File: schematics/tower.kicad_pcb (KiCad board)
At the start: 2 copper layers, 50.8 x 48.3 mm, 17 parts, among them IC1 ESP32-SOLO-1, J1 Conn_01x02, J2 Conn_01x06, J3 Conn_01x09, J4 Conn_02x10_Odd_Even, SW1 SW_Push, SW2 SW_SPDT, U1 NCP1117-3.3_SOT223

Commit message: finished (I think) schematics for tower and controller
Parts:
- removed the REF** at (127.0, 119.4)
- removed the REF** at (170.2, 116.8)
- removed the REF** at (127.0, 80.0)
- removed U1: NCP1117-3.3_SOT223, Package_TO_SOT_SMD:SOT-223-3_TabPin2
- added C5: 100nF, Capacitor_SMD:C_0805_2012Metric, B.Cu at (150.4, 61.5)
- added C6: 100nF, Capacitor_SMD:C_0805_2012Metric, F.Cu at (186.7, 58.4)
- added C7: 100nF, Capacitor_SMD:C_0805_2012Metric, F.Cu at (180.3, 86.4)
- added D1: BAT760-7, Mouser:SOD2513X120N, F.Cu at (125.7, 68.6)
- added D2: LED, Mouser:APHCM2012QBCDF01, F.Cu at (118.6, 65.5)
- added J5: Conn_02x10_Odd_Even, Connector_PinSocket_2.54mm:PinSocket_2x10_P2.54mm_Vertical, F.Cu at (188.0, 62.2)
- added Q1: SS8050-G, Mouser:SOT95P240X115-3N, F.Cu at (152.4, 82.5)
- added Q2: SS8050-G, Mouser:SOT95P240X115-3N, F.Cu at (157.5, 82.5)
- added R3: 10k, Resistor_SMD:R_0805_2012Metric, F.Cu at (154.9, 86.4)
- added R4: 10k, Resistor_SMD:R_0805_2012Metric, F.Cu at (139.7, 66.0)
- added R5: 10k, Resistor_SMD:R_0805_2012Metric, F.Cu at (139.7, 58.4)
- added R6: 0, Resistor_SMD:R_0201_0603Metric, F.Cu at (121.9, 65.0)
- added R7: 0, Resistor_SMD:R_0201_0603Metric, F.Cu at (130.8, 62.2)
- added REF**: MountingHole_3.2mm_M3, MountingHole:MountingHole_3.2mm_M3, F.Cu at (133.3, 71.9)
- added REF**: MountingHole_3.2mm_M3, MountingHole:MountingHole_3.2mm_M3, F.Cu at (197.4, 61.5)
- added REF**: MountingHole_3.2mm_M3, MountingHole:MountingHole_3.2mm_M3, F.Cu at (197.1, 110.5)
- added REF**: MountingHole_3.2mm_M3, MountingHole:MountingHole_3.2mm_M3, F.Cu at (107.7, 110.5)
- C1, C2: value 100nF -> 0.1uF
- C4: value 100nF -> 22uF; moved to B.Cu
- IC1: footprint RF_Module:ESP32-WROOM-32 -> Mouser:ESP32SOLO1
- J1: value Conn_01x02 -> 216990-0003; footprint Connector_PinHeader_1.00mm:PinHeader_1x02_P1.00mm_Vertical -> Mouser:2169900003
- J3: value Conn_01x09 -> Conn_01x05; footprint Connector_PinSocket_1.00mm:PinSocket_1x09_P1.00mm_Vertical -> Connector_PinSocket_2.54mm:PinSocket_1x05_P2.54mm_Vertical
- J4: value Conn_02x10_Odd_Even -> SD_Card; footprint Connector_PinSocket_2.54mm:PinSocket_2x10_P2.54mm_Vertical -> Connector_Card:SD_Kyocera_145638109211859+
- R1: value 10k -> 20
- SW1: footprint Button_Switch_THT:SW_TH_Tactile_Omron_B3F-10xx -> Button_Switch_SMD:SW_SPST_CK_KXT3
- SW2: value SW_SPDT -> SW_Push; footprint Button_Switch_THT:SW_Slide_1P2T_CK_OS102011MS2Q -> Button_Switch_SMD:SW_SPST_CK_KXT3
- moved J4 57.5 mm to (114.3, 92.7), turned to 270 degrees
- moved C4 50.1 mm to (150.4, 58.4), turned to 0 degrees
- moved J1 40.6 mm to (107.4, 66.0), turned to 270 degrees
- moved C3 38.9 mm to (139.7, 62.2)
- moved R1 37.3 mm to (119.4, 68.6), turned to 180 degrees
- moved SW1 30.1 mm to (165.1, 82.5), turned to 180 degrees
- moved C1 28.5 mm to (165.1, 88.9), turned to 0 degrees
- moved SW2 28.0 mm to (144.8, 82.5), turned to 0 degrees
- moved J2 27.9 mm to (152.4, 97.8), turned to 90 degrees
- moved J3 26.2 mm to (121.9, 59.7), turned to 90 degrees
- moved IC1 24.4 mm to (154.9, 63.5)
- moved C2 17.3 mm to (144.8, 88.9)
- moved R2 14.0 mm to (154.9, 90.2)
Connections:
- net AUDIO_L renamed Net-(J4-Pad9)
- C1 pad 1: GND -> GPIO0
- C1 pad 2: Net-(C1-Pad2) -> GND
- C2 pad 1: GND -> EN
- C2 pad 2: Vcc -> GND
- C3 pad 1: GND -> EN
- C3 pad 2: Vcc -> GND
- C4 pad 1: GND -> VOUT
- C4 pad 2: 5V -> GND
- IC1 pad 10: IO25 -> SDMOSI
- IC1 pad 11: IO26 -> SDCLK
- IC1 pad 12: IO27 -> SDMISO
- IC1 pad 13: PDN -> Net-(IC1-Pad13)
- IC1 pad 2: Vcc -> VOUT
- IC1 pad 23: GPIO2 -> Net-(IC1-Pad23)
- IC1 pad 24: Net-(IC1-Pad24) -> GPIO2
- IC1 pad 25: Net-(IC1-Pad25) -> GPIO0
- IC1 pad 26: Net-(IC1-Pad26) -> GPIO1
- IC1 pad 28: DTR -> Net-(IC1-Pad28)
- IC1 pad 29: CTS -> Net-(IC1-Pad29)
- IC1 pad 3: Net-(C1-Pad2) -> EN
- IC1 pad 36: GPIO1 -> Net-(IC1-Pad36)
- J2 pad 3: Vcc -> VOUT
- J3 pad 1: Vcc -> VOUT
- J3 pad 3: IO34 -> 5V
- J3 pad 4: IO35 -> SHDN
- J3 pad 5: IO32 -> PG
- J4 pad 1: Vcc -> Net-(J4-Pad1)
- J4 pad 10: NC -> Net-(J4-Pad10)
- J4 pad 11: GPIO0 -> Net-(J4-Pad11)
- J4 pad 12: GPIO1 -> Net-(J4-Pad12)
- J4 pad 13: GPIO2 -> Net-(J4-Pad13)
- J4 pad 2: GND -> SDMOSI
- J4 pad 3: SCK -> GND
- J4 pad 4: MISO -> VOUT
- J4 pad 5: MOSI -> SDCLK
- J4 pad 6: CS -> GND
- J4 pad 7: INT -> SDMISO
- J4 pad 8: PDN -> Net-(J4-Pad8)
- R1 pad 1: Net-(C1-Pad2) -> Net-(D1-Pad2)
- R1 pad 2: Vcc -> Net-(J1-PadA4)
- R2 pad 1: Net-(IC1-Pad25) -> DTR
- R2 pad 2: Net-(R2-Pad2) -> Net-(Q1-Pad1)
- SW1 pad 2: Vcc -> GPIO0
- SW2 pad 1: Net-(R2-Pad2) -> GND
- SW2 pad 2: Vcc -> EN
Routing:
- net GND: track 161.6 -> 14.6 mm, vias 5 -> 9
- net VOUT: track 0.00 -> 146.3 mm, vias 0 -> 5
- net Vcc: track 136.8 -> 0.00 mm, vias 1 -> 0
- net 5V: track 59.5 -> 126.9 mm, vias 0 -> 2
- net EN: track 0.00 -> 47.6 mm
- net SDMISO: track 0.00 -> 41.3 mm, vias 0 -> 2
- net SDCLK: track 0.00 -> 34.8 mm, vias 0 -> 2
- net PDN: track 32.9 -> 0.00 mm, vias 1 -> 0
- net GPIO0: track 31.6 -> 62.7 mm, vias 2 -> 0
- net SDMOSI: track 0.00 -> 28.6 mm, vias 0 -> 2
- net Net-(C1-Pad2): track 27.7 -> 0.00 mm, vias 2 -> 0
- net TX: track 18.2 -> 41.2 mm, vias 0 -> 1
- net RX: track 18.3 -> 39.5 mm, vias 0 -> 1
- net DTR: track 0.00 -> 15.8 mm
- net Net-(R2-Pad2): track 15.7 -> 0.00 mm, vias 1 -> 0
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- added copper zone on B.Cu, net GND
- added copper zone on F.Cu, net GND
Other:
- board size 50.8 x 48.3 mm -> 100.1 x 58.2 mm
- board text added: "+"
- board text added: "-"
- board text added: "5V"
- board text added: "GND"
- board text added: "PG"
- board text added: "Purdue University ECE 477: Senior Design Group 6: Mario Kart 3/1/2022 Tower PCB Version: 1.0 Authors: Andre Hatushikano Da Yeon Nam Jake Doan Jorge Apolo"
- board text added: "VOUT"

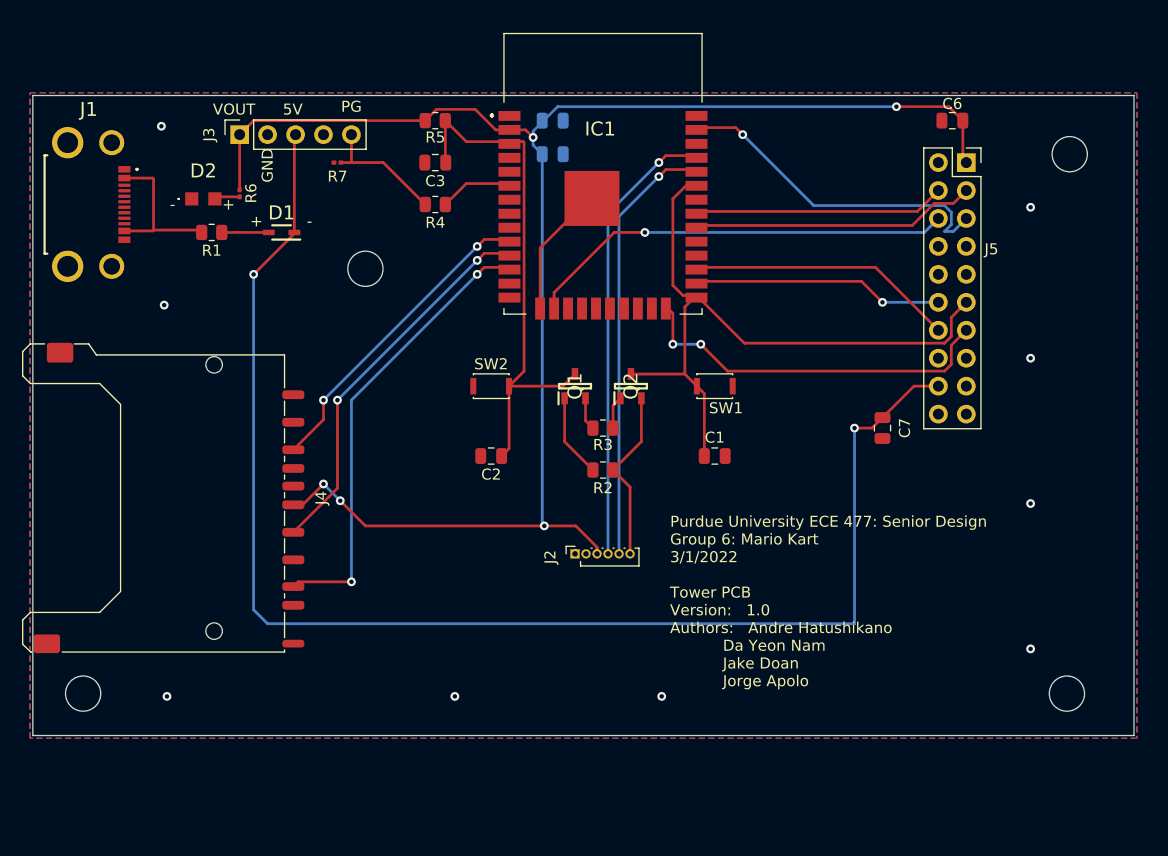
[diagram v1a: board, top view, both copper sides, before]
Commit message: converted all schematics into kicad6 format
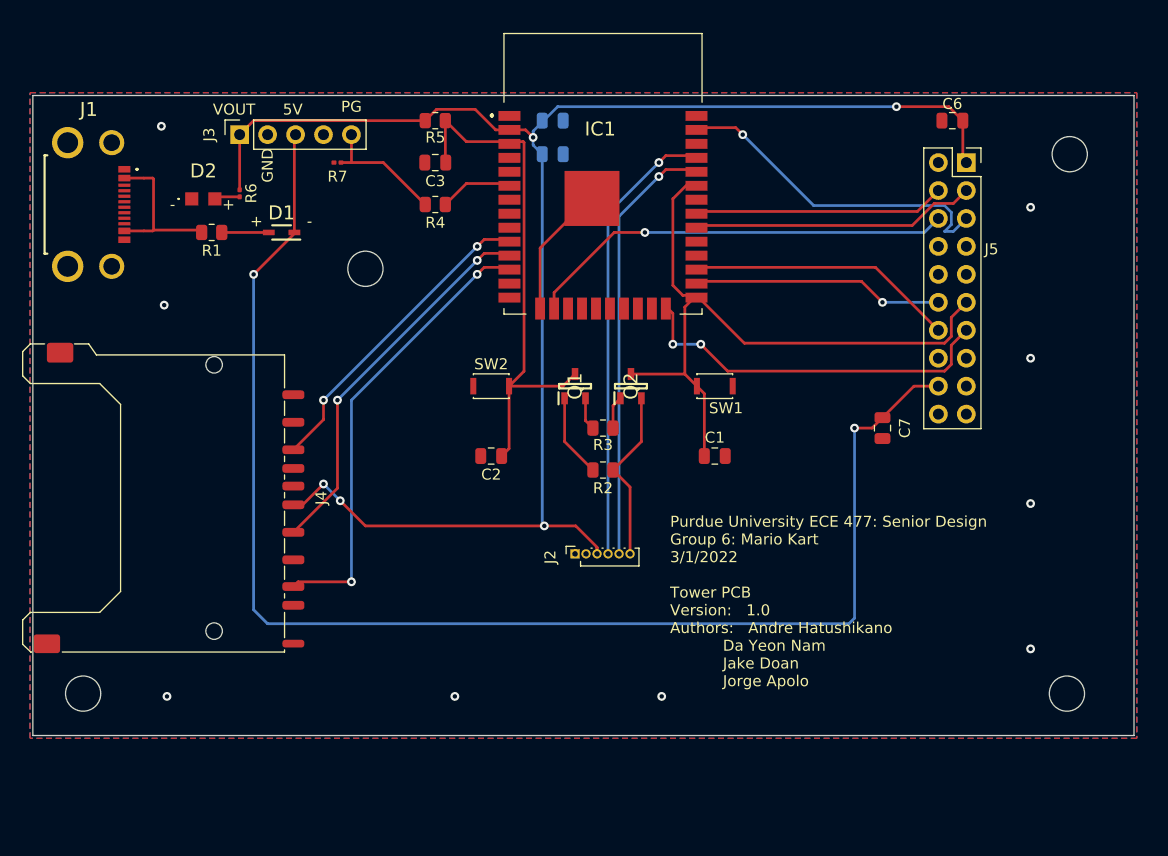
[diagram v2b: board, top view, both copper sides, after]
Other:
- net class Default removed

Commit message: think Ive finished the schematics
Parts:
- IC1: footprint Mouser:ESP32SOLO1 -> RF_Module:ESP32-WROOM-32
- J2: footprint Connector_PinSocket_1.00mm:PinSocket_1x06_P1.00mm_Vertical -> Connector_PinSocket_2.54mm:PinSocket_1x06_P2.54mm_Vertical
- R6, R7: footprint Resistor_SMD:R_0201_0603Metric -> Resistor_SMD:R_0805_2012Metric
- moved J2 8.12 mm to (145.0, 101.2)
- moved IC1 2.34 mm to (154.2, 65.7)
- moved R7 1.59 mm to (131.1, 63.8)
- moved J4 1.39 mm to (115.7, 92.5)
- moved D2 1.29 mm to (117.5, 65.0)
- moved R6 1.07 mm to (121.9, 64.0)
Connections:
- IC1 pad 13: Net-(IC1-Pad13) -> unconnected-(IC1-Pad13)
- IC1 pad 14: Net-(IC1-Pad14) -> unconnected-(IC1-Pad14)
- IC1 pad 17: Net-(IC1-Pad17) -> unconnected-(IC1-Pad17)
- IC1 pad 18: Net-(IC1-Pad18) -> unconnected-(IC1-Pad18)
- IC1 pad 19: Net-(IC1-Pad19) -> unconnected-(IC1-Pad19)
- IC1 pad 20: Net-(IC1-Pad20) -> unconnected-(IC1-Pad20)
- IC1 pad 21: Net-(IC1-Pad21) -> unconnected-(IC1-Pad21)
- IC1 pad 22: Net-(IC1-Pad22) -> unconnected-(IC1-Pad22)
- IC1 pad 23: Net-(IC1-Pad23) -> unconnected-(IC1-Pad23)
- IC1 pad 28: Net-(IC1-Pad28) -> unconnected-(IC1-Pad28)
- IC1 pad 29: Net-(IC1-Pad29) -> unconnected-(IC1-Pad29)
- IC1 pad 32: Net-(IC1-Pad32) -> unconnected-(IC1-Pad32)
- IC1 pad 36: Net-(IC1-Pad36) -> unconnected-(IC1-Pad36)
- IC1 pad 4: Net-(IC1-Pad4) -> unconnected-(IC1-Pad4)
- IC1 pad 5: Net-(IC1-Pad5) -> unconnected-(IC1-Pad5)
- J1 pad A5: Net-(J1-PadA5) -> unconnected-(J1-PadA5)
- J1 pad A6: Net-(J1-PadA6) -> unconnected-(J1-PadA6)
- J1 pad A7: Net-(J1-PadA7) -> unconnected-(J1-PadA7)
- J1 pad A8: Net-(J1-PadA8) -> unconnected-(J1-PadA8)
- J1 pad B5: Net-(J1-PadB5) -> unconnected-(J1-PadB5)
- J1 pad B6: Net-(J1-PadB6) -> unconnected-(J1-PadB6)
- J1 pad B7: Net-(J1-PadB7) -> unconnected-(J1-PadB7)
- J1 pad B8: Net-(J1-PadB8) -> unconnected-(J1-PadB8)
- J1 pad MH1: Net-(J1-PadMH1) -> unconnected-(J1-PadMH1)
- J1 pad MH2: Net-(J1-PadMH2) -> unconnected-(J1-PadMH2)
- J1 pad MH3: Net-(J1-PadMH3) -> unconnected-(J1-PadMH3)
- J1 pad MH4: Net-(J1-PadMH4) -> unconnected-(J1-PadMH4)
- J4 pad 1: Net-(J4-Pad1) -> unconnected-(J4-Pad1)
- J4 pad 10: Net-(J4-Pad10) -> unconnected-(J4-Pad10)
- J4 pad 11: Net-(J4-Pad11) -> unconnected-(J4-Pad11)
- J4 pad 12: Net-(J4-Pad12) -> unconnected-(J4-Pad12)
- J4 pad 13: Net-(J4-Pad13) -> unconnected-(J4-Pad13)
- J4 pad 8: Net-(J4-Pad8) -> unconnected-(J4-Pad8)
- J4 pad 9: Net-(J4-Pad9) -> unconnected-(J4-Pad9)
- Q1 pad 2: RTS -> CTS
- R3 pad 1: RTS -> CTS
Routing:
- net CTS: track 0.00 -> 21.4 mm, vias 0 -> 1
- net GND: track 14.6 -> 0.77 mm, vias 9 -> 10
- net TX: track 41.2 -> 45.1 mm
- net DTR: track 15.8 -> 19.4 mm
- net RX: track 39.5 -> 42.7 mm
- net RTS: track 2.99 -> 0.00 mm
- net SDMISO: track 41.3 -> 39.3 mm
- net MOSI: track 30.8 -> 28.8 mm
- net SDCLK: track 34.8 -> 33.5 mm
- net SDMOSI: track 28.6 -> 27.2 mm, vias 2 -> 0
- net GPIO0: track 62.7 -> 63.9 mm
- net Net-(D2-Pad2): track 2.33 -> 3.48 mm
- net GPIO1: track 22.9 -> 23.8 mm
- net GPIO3: track 24.3 -> 25.2 mm
- net Net-(J1-PadA4): track 14.5 -> 13.7 mm
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
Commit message: final pcbs and schematics
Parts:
- added R8: 10k, Resistor_SMD:R_0805_2012Metric, F.Cu at (139.7, 60.8)
- J1: value 216990-0003 -> USB_B_Micro; footprint Mouser:2169900003 -> Connector_USB:USB_Micro-B_Molex-105017-0001
- R1: value 20 -> 10k
- REF** (x4): value MountingHole_3.2mm_M3 -> MountingHole_3.2mm_M3_DIN965_Pad; footprint MountingHole:MountingHole_3.2mm_M3 -> MountingHole:MountingHole_3.2mm_M3_DIN965_Pad
- moved J1 97.6 mm to (198.8, 100.4), turned to 90 degrees
- moved D1 75.9 mm to (191.9, 105.7), turned to 0 degrees
- moved J3 74.3 mm to (177.1, 109.4)
- moved R6 67.1 mm to (175.0, 105.1), turned to 90 degrees
- moved D2 64.2 mm to (169.6, 102.4)
- moved R1 61.1 mm to (180.3, 63.7), turned to 0 degrees
- moved REF** 25.8 mm to (107.6, 73.4)
- moved R7 4.49 mm to (135.0, 66.0)
- moved C7 3.95 mm to (181.7, 82.6), turned to 0 degrees
- moved C3 0.98 mm to (139.7, 63.2)
- moved IC1 0.35 mm to (154.3, 65.4)
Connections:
- D1 pad 2: Net-(D1-Pad2) -> Net-(J1-Pad1)
- J2 pad 3: VOUT -> unconnected-(J2-Pad3)
- R1 pad 1: Net-(D1-Pad2) -> GPIO0
- R1 pad 2: Net-(J1-PadA4) -> VOUT
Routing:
- net 5V: track 126.6 -> 39.4 mm, vias 2 -> 0
- net PG: track 12.4 -> 90.6 mm, vias 0 -> 2
- net VOUT: track 146.7 -> 164.1 mm, vias 5 -> 4
- net GPIO0: track 63.9 -> 80.6 mm
- net NC: track 0.00 -> 13.8 mm
- net Net-(J1-PadA4): track 13.7 -> 0.00 mm
- net Net-(J1-Pad1): track 0.00 -> 6.58 mm
- net Net-(D1-Pad2): track 4.28 -> 0.00 mm
- net Net-(D2-Pad2): track 3.48 -> 5.03 mm
- net GND: track 0.77 -> 2.21 mm, vias 10 -> 15
- net EN: track 47.0 -> 48.0 mm
- net SDMISO: vias 2 -> 0
- net SDCLK: vias 2 -> 0
